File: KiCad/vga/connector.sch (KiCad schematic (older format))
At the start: 14 parts, among them J1 VGA connector, U20 74HC00, X2 Edge72

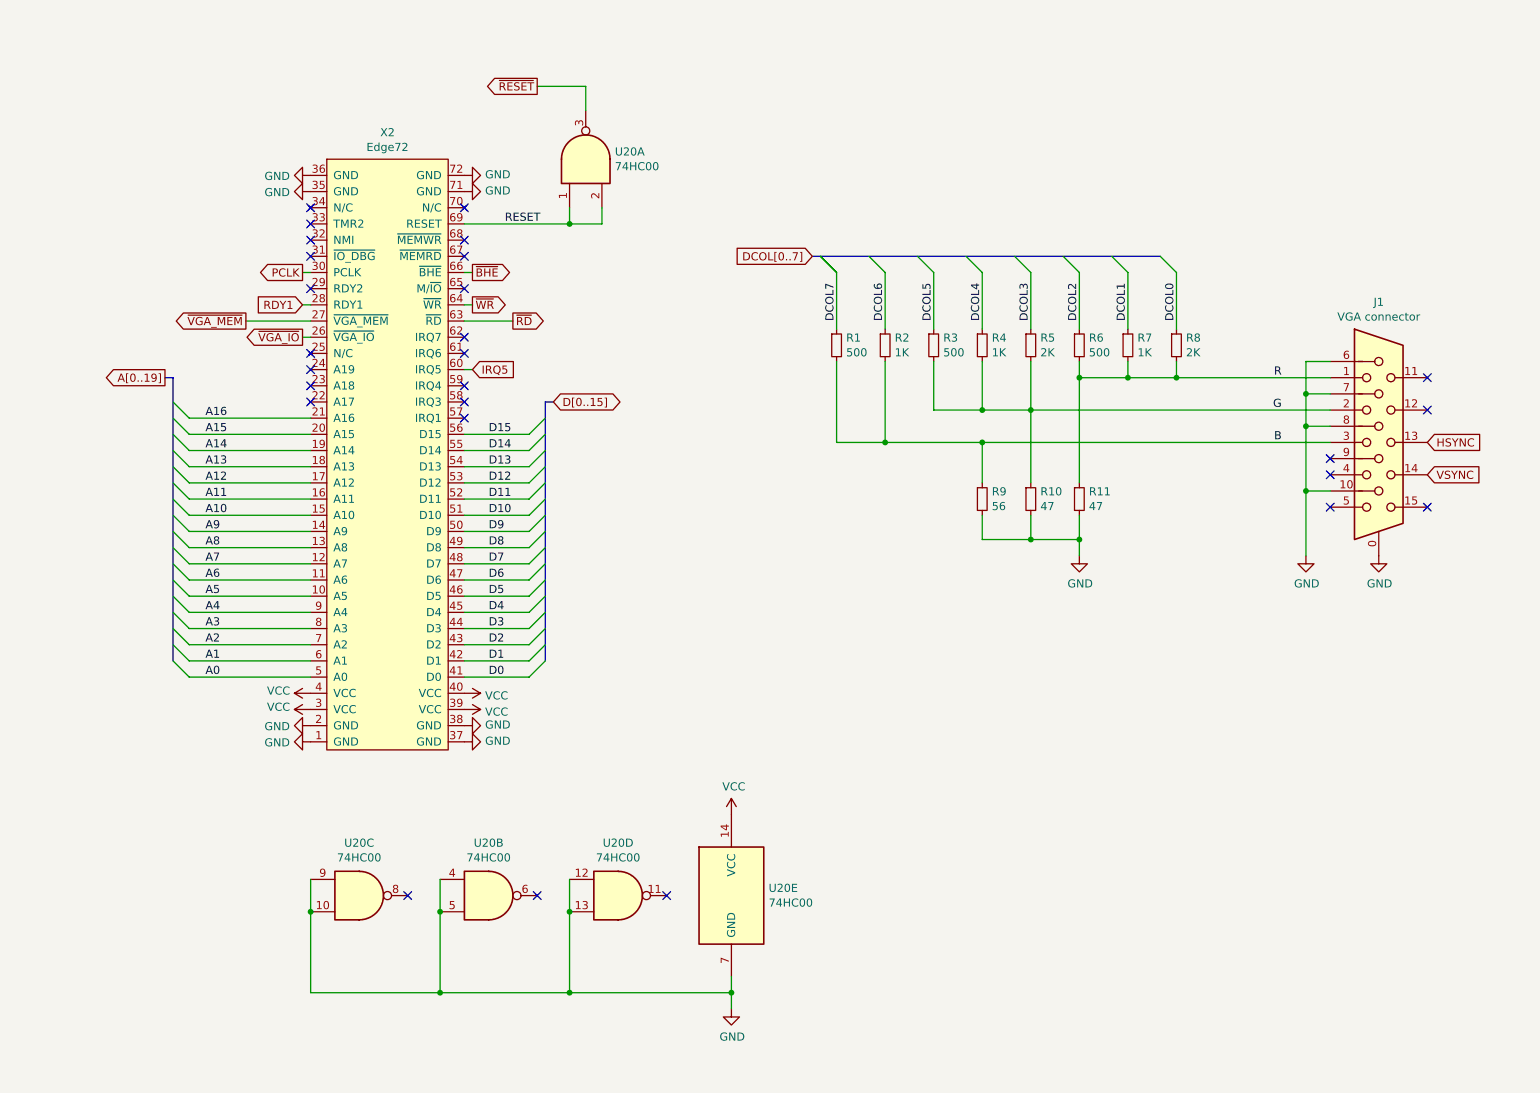
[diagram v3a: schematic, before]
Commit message: Replaced MAX7000 CPLD with MAX II in graphics adapter. PCB redesign with smaller size.
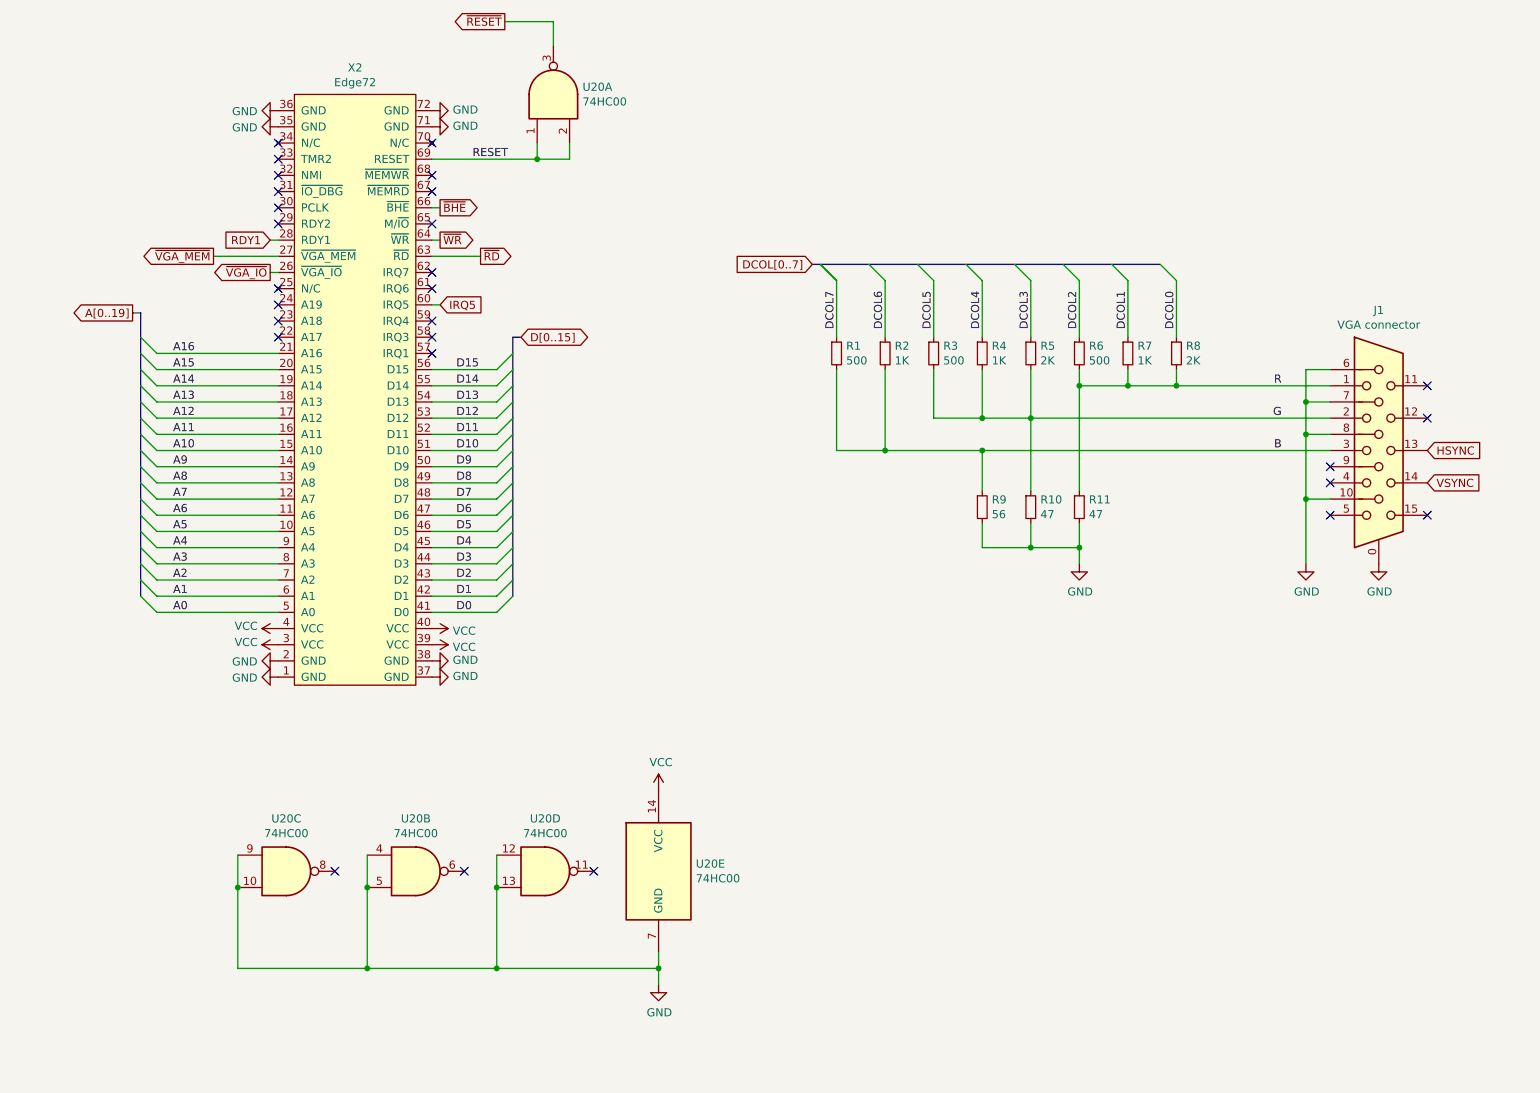
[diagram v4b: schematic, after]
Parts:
- R1, R10, R11, R2, R3, R4, R5, R6, R7, R8, R9: footprint Resistor_THT:R_Axial_DIN0204_L3.6mm_D1.6mm_P7.62mm_Horizontal -> Resistor_THT:R_Axial_DIN0207_L6.3mm_D2.5mm_P7.62mm_Horizontal
- U20: footprint Package_DIP:DIP-14_W7.62mm_LongPads -> Package_SO:SOIC-14_3.9x8.7mm_P1.27mm
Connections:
- net PCLK: no longer names the net of X2.30 (PCLK)
- no-connect marks 27 -> 28
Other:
- moved on the sheet: J1, R1, R10, R11, R2, R3, R4, R5, R6, R7, R8, R9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

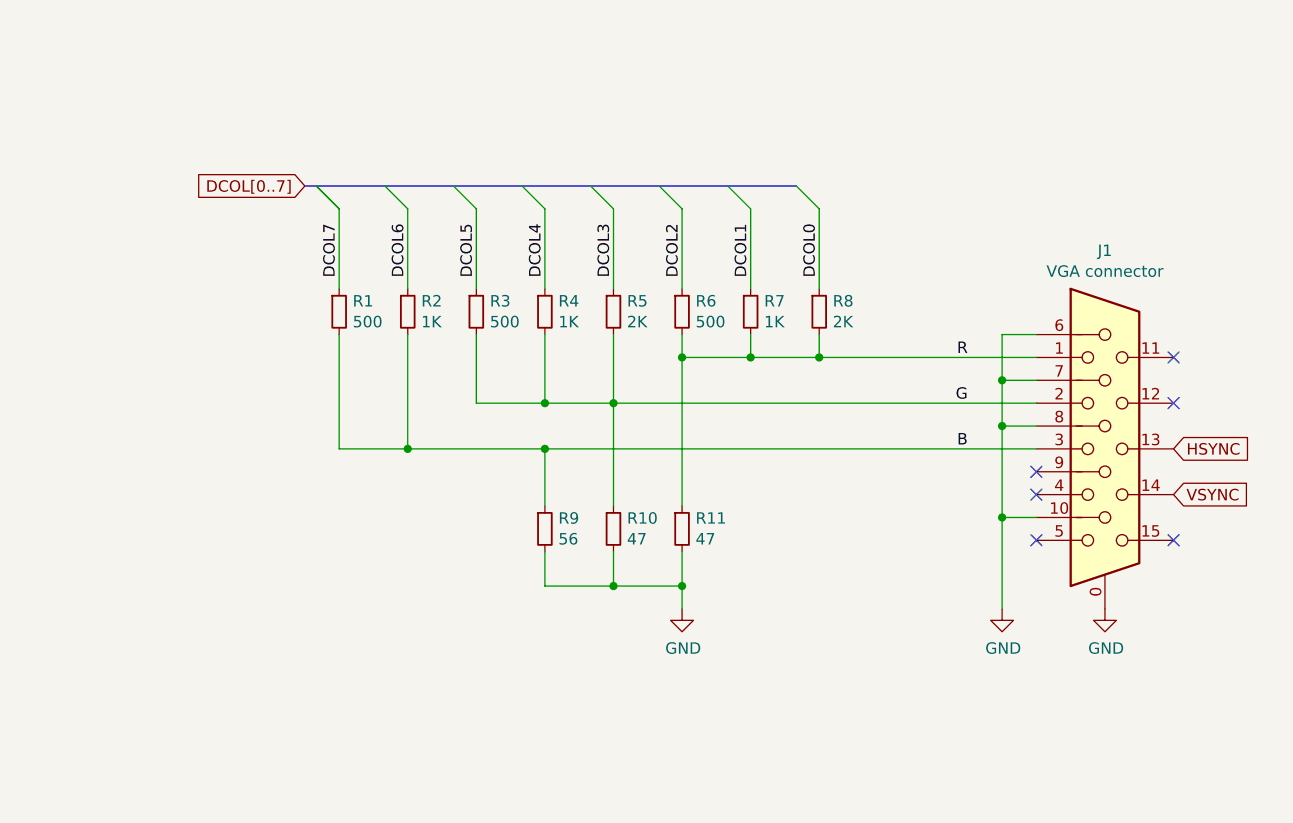
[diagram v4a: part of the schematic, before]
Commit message: Finished VGA adapter Rev. 1.0
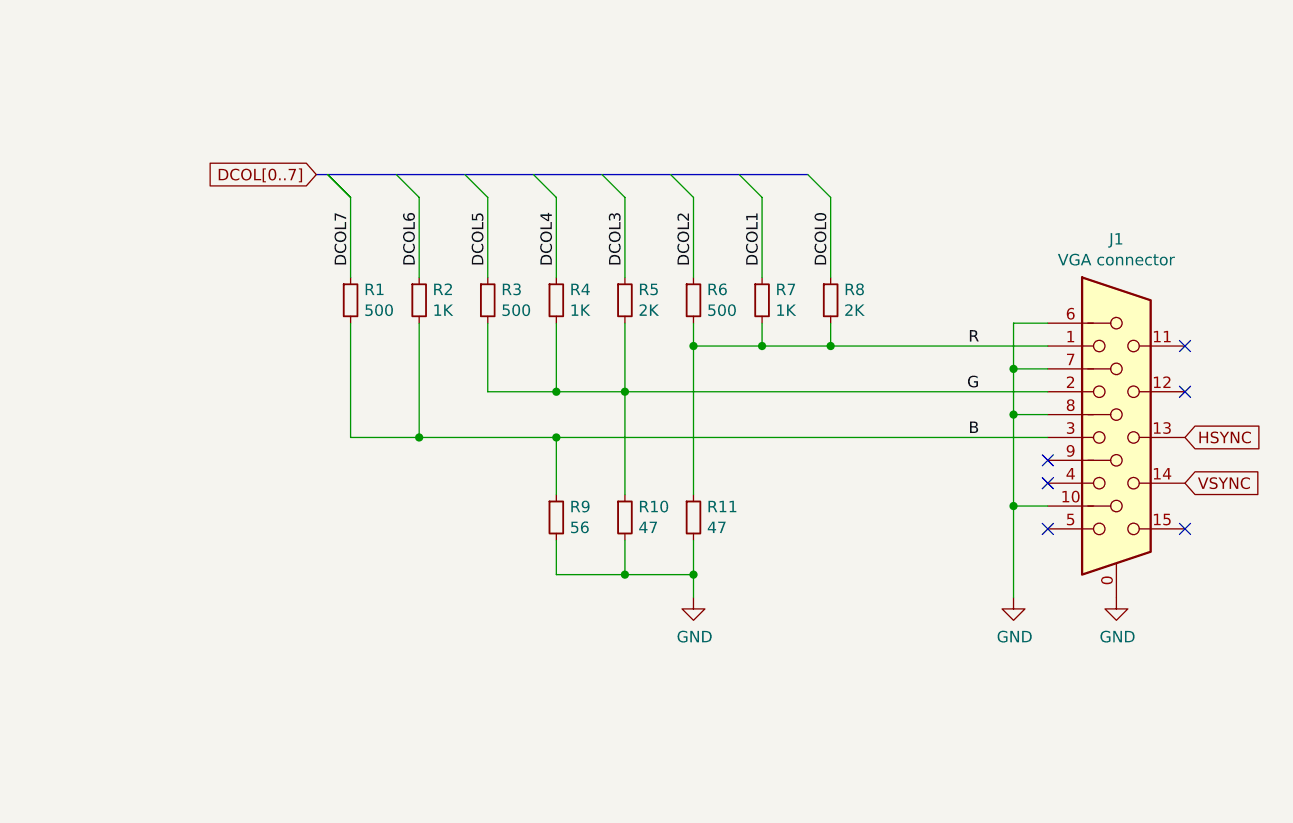
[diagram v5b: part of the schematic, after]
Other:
- moved on the sheet: J1, R1, R10, R11, R2, R3, R4, R5, R6, R7, R8, R9

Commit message: Updated KiCad versioning information in schematics. Fixed button wrong pinout in backplane. Added missing files to git.
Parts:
- X2: symbol Mini8086:Edge72 -> vga-rescue:Edge72-Mini8086
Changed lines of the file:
@@
 encoding utf-8
 Sheet 6 7
-Title ""
+Title "Mini8086 VGA board"
 Date ""
-Rev ""
+Rev "1.1"
 Comp ""
 Comment1 ""
@@
 NoConn ~ 3600 1950
 $Comp
-L Mini8086:Edge72 X2
+L vga-rescue:Edge72-Mini8086 X2
 U 1 1 5F84BE1E
 P 3100 3450
